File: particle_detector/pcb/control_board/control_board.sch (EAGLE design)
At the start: 35 parts, among them IC1 LT1807R, IC2 SENSL-SIPM, IC3 LT3461, IC4 TEENSY_3.2_NO_BOTTOM

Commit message: move to eagle project; fix vcc/3.3v and ind package; remove full board design
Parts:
- removed C10, C11, C12, C13: (no value), rcl:C-EUC0805K
- removed IC2: SENSL-SIPM, personal:SENSL-SIPM
- removed R11, R12: (no value), rcl:R-EU_M0805
- removed XCHIP: (no value), personal:XCHIP-1X5
- added I2C: (no value), pinhead:PINHD-1X5
- added SIPM: (no value), pinhead:PINHD-2X3
- added XBUS: (no value), personal:XINABOX-XBUS
- C1: value (none) -> 22pF
- C2: value (none) -> 0.47uF
- C3, C4: value (none) -> 1uF
- C5: value (none) -> 10pF
- C6: value (none) -> 10uF
- C7: value (none) -> 0.1uF
- C8: value (none) -> 20nF
- C9, R10: value (none) -> sh
- D1, D2: value B340A -> MBR0540
- IC4: value TEENSY_3.2_NO_BOTTOM -> TEENSY 3.2
- L1: value (none) -> 47uH; device rcl:L-USL2012C -> rcl:L-USL3225M
- L2: value (none) -> 2.5k
- R1, R5, R6: value (none) -> 10k
- R2: value (none) -> 226k
- R3: value (none) -> 1k
- R4: value (none) -> 249
- R7, R8: value (none) -> 100k
- R9: value (none) -> 24.9k
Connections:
- removed net N$5: C11.1, C12.1, C13.1, IC2.CATHODE, R12.2
- removed net N$6: C10.1, R11.2, R12.1
- new net 3.3V: C6.1, C7.1, I2C.4, IC1P.V+, IC4.3.3V, XBUS.3.3V
- new net AGND: C6.2, C7.2, C8.2, IC1P.V-, IC4.AGND, R4.1, R6.1, R7.1, R9.1
- new net SCL: I2C.1, IC4.19/A5/T/SCL0, XBUS.SCL
- new net SDA: I2C.2, IC4.18/A4/T/SDA0, XBUS.SDA
- new net VBAT: XBUS.VBAT
- net GND: now also I2C.3, SIPM.3, SIPM.4, XBUS.GND; no longer C10.2, C11.2, C12.2, C13.2, C6.2, C7.2, C8.2, IC1P.V-, R4.1, R6.1, R7.1, R9.1
- net HV: now also SIPM.1, SIPM.2; no longer R11.1
- net SIGNAL: now also SIPM.5, SIPM.6; no longer IC2.ANODE
- net VCC: now also I2C.5; no longer C6.1, C7.1, IC1P.V+
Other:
- note removed: "SiPM PCB"
- moved on the sheet: C1, C5, IC1P, R4

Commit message: Stuck the TLV on there, not finished
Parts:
- added C10, C11: (no value), rcl:C-EUC0805
- added R11, R12: (no value), resistor:R-EU_M0805
- added U$1: TLV3501, AU_Thinsat_Comparators:TLV3501
- IC1: device personal:LT1807R -> Personal:LT1807R
- IC3: device personal:LT3461 -> Personal:LT3461
- IC4: device personal:TEENSY_3.2_NO_BOTTOM -> Personal:TEENSY_3.2_NO_BOTTOM
- XBUS: device personal:XINABOX-XBUS -> Personal:XINABOX-XBUS
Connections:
- new net INT_TRIG: IC4.22/A8/T/PWM, U$1.OUT
- new net N$5: R11.2, R12.2, U$1.IN-
- net 3.3V: now also C10.1, C11.1, R12.1, U$1.V+
- net GND: now also C10.2, C11.2, R11.1, U$1.SHDN, U$1.V-
- net SIG_PEAK: now also U$1.IN+
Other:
- moved on the sheet: I2C, TOUCH, XBUS

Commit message: reroute traces and fix footprint for TLV chip
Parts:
- removed U$1: TLV3501, AU_Thinsat_Comparators:TLV3501
- added IC2: TLV3501, AU_Thinsat_Comparators:TLV3501
- C10: value (none) -> 10uF
- C11: value (none) -> 0.1uF
- IC1: device Personal:LT1807R -> personal:LT1807R
- IC3: device Personal:LT3461 -> personal:LT3461
- IC4: device Personal:TEENSY_3.2_NO_BOTTOM -> personal:TEENSY_3.2_NO_BOTTOM
- R11: value (none) -> 1k
- R12: value (none) -> 100k
- TOUCH: device pinhead:PINHD-1X3 -> pinhead:PINHD-1X4
- XBUS: device Personal:XINABOX-XBUS -> personal:XINABOX-XBUS
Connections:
- removed net INT_TRIG: IC4.22/A8/T/PWM, U$1.OUT
- new net SIG_INT: IC2.OUT, IC4.22/A8/T/PWM, TOUCH.4
- net 3.3V: now also IC2.V+; no longer U$1.V+
- net AGND: now also C10.2, C11.2, IC2.SHDN, IC2.V-, R11.1
- net GND: no longer C10.2, C11.2, R11.1, U$1.SHDN, U$1.V-
- net N$5: now also IC2.IN-; no longer U$1.IN-
- net SIG_PEAK: now also IC2.IN+; no longer U$1.IN+
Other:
- note added: "Authors: Kristof Aldenderfer, Jacob VanCampen"
- note added: "Detector Board Header"
- note added: "I2C and Xinabox Header"
- note added: "Interrupt Generation"
- note removed: "Author: Kristof Aldenderfer Forked from Cosmic Watch v2"
- moved on the sheet: C10, C11, C5, C6, C7, C8, C9, D1, D2, I2C, IC1A, IC1B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

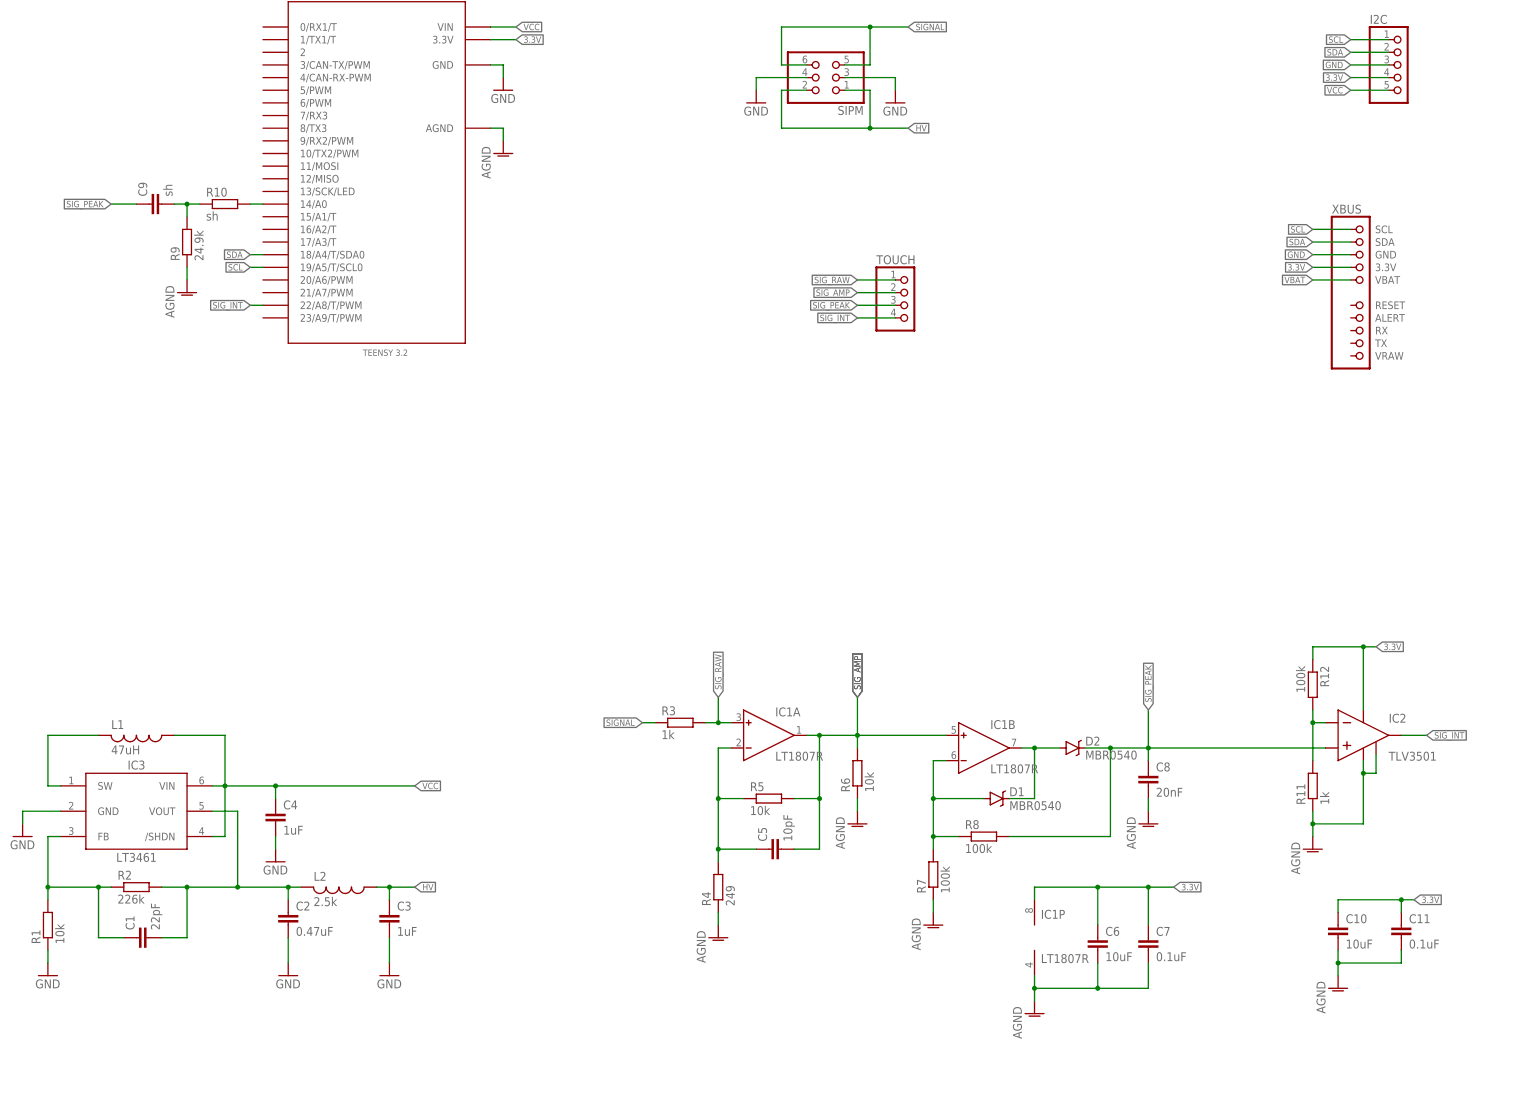
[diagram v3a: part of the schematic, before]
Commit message: remove VCC traces to DC-DC booster; 3.3V traces remain unrouted
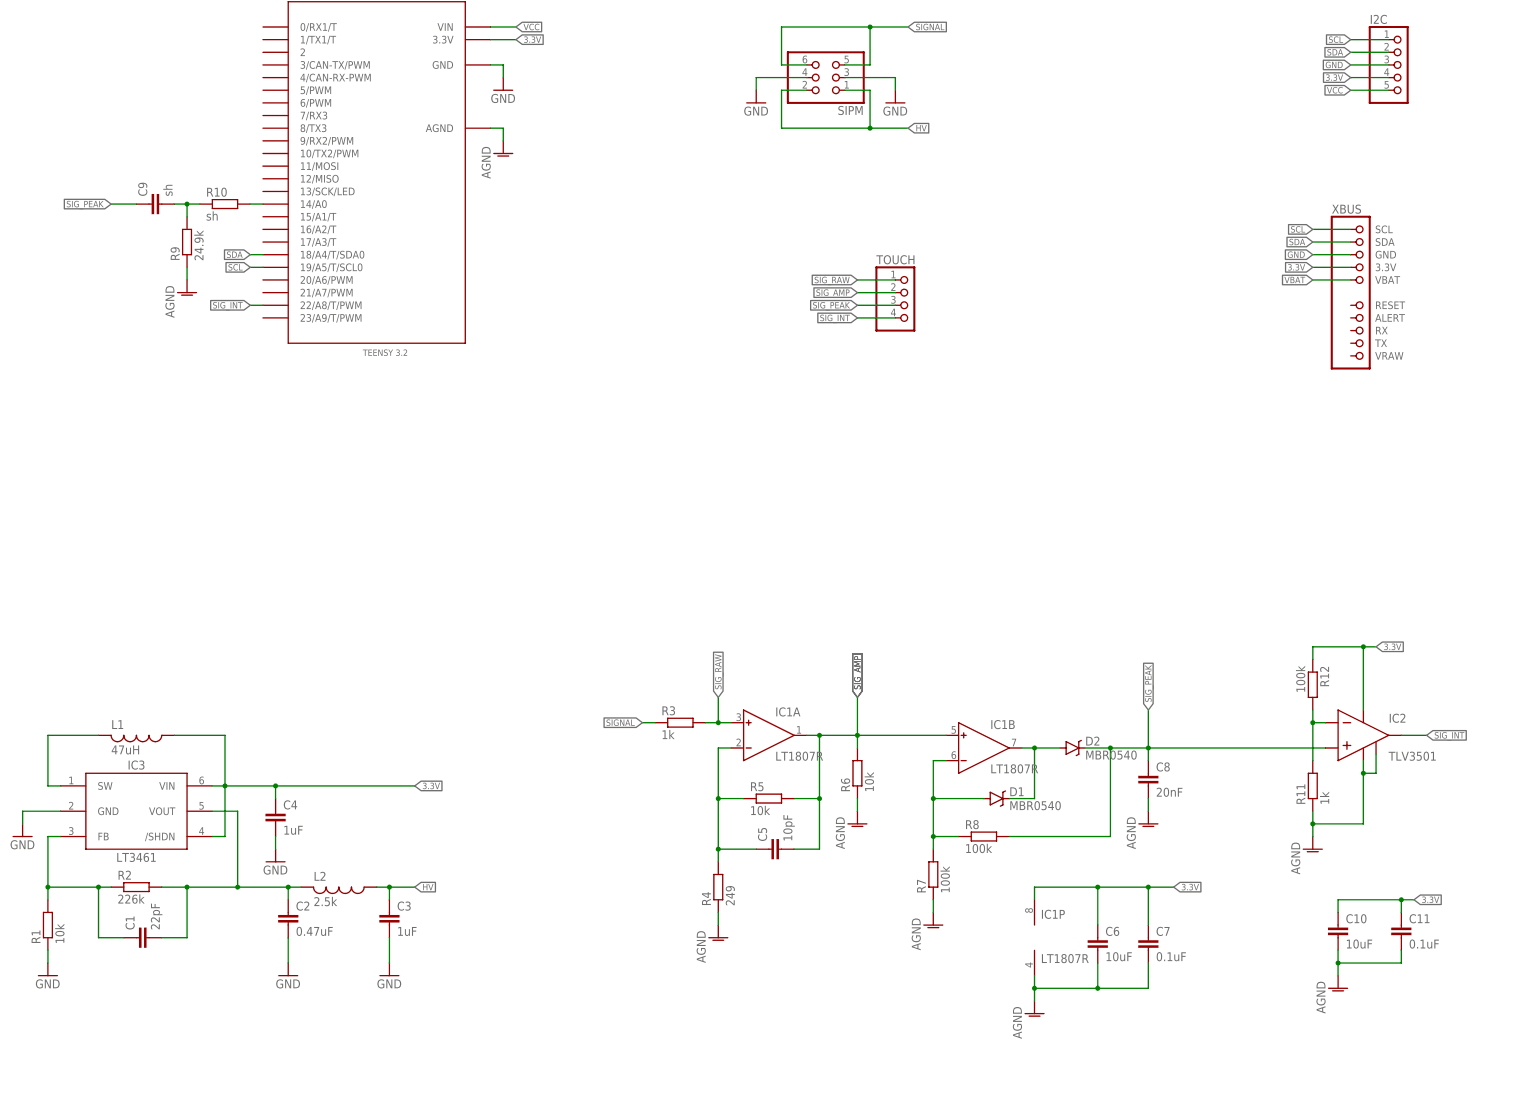
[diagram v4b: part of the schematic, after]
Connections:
- net 3.3V: now also C4.1, IC3./SHDN, IC3.VIN, L1.1
- net VCC: no longer C4.1, IC3./SHDN, IC3.VIN, L1.1

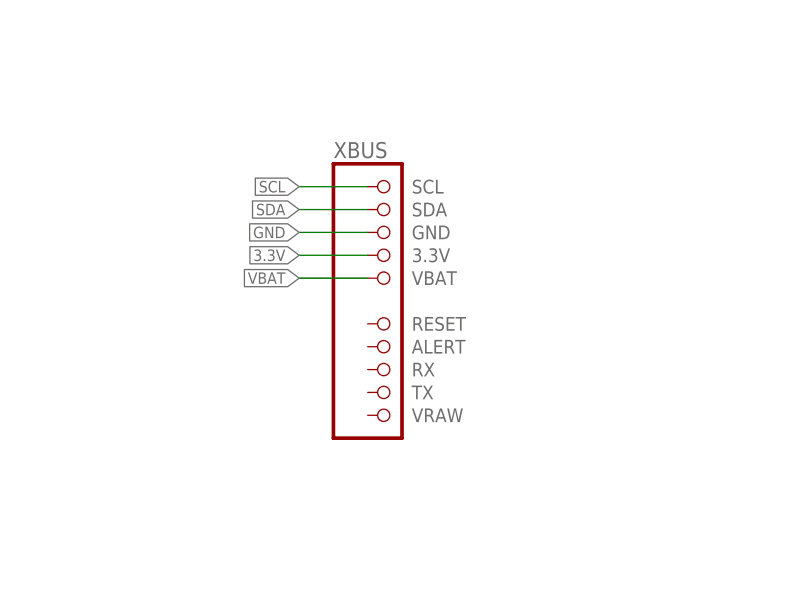
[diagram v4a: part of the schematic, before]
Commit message: adjust comparator footprint; route 3.3V traces. send to fab
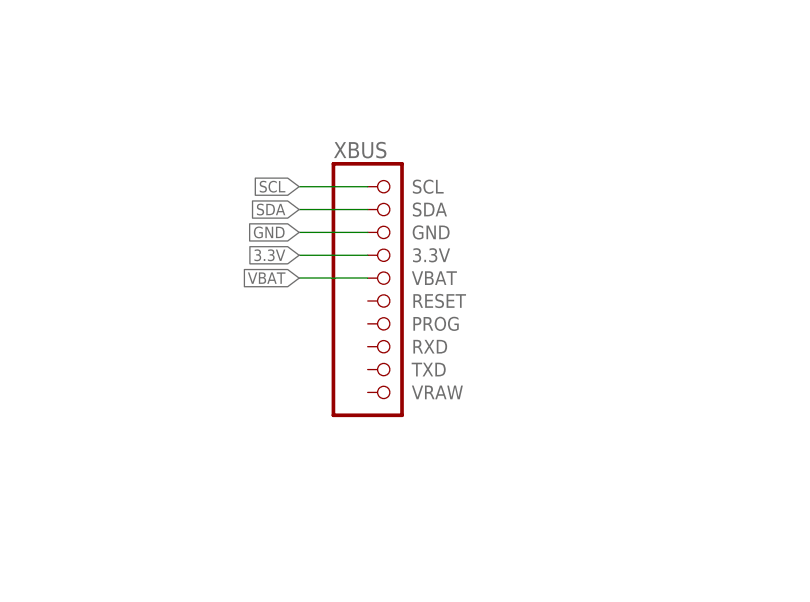
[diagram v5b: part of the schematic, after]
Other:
- moved on the sheet: XBUS

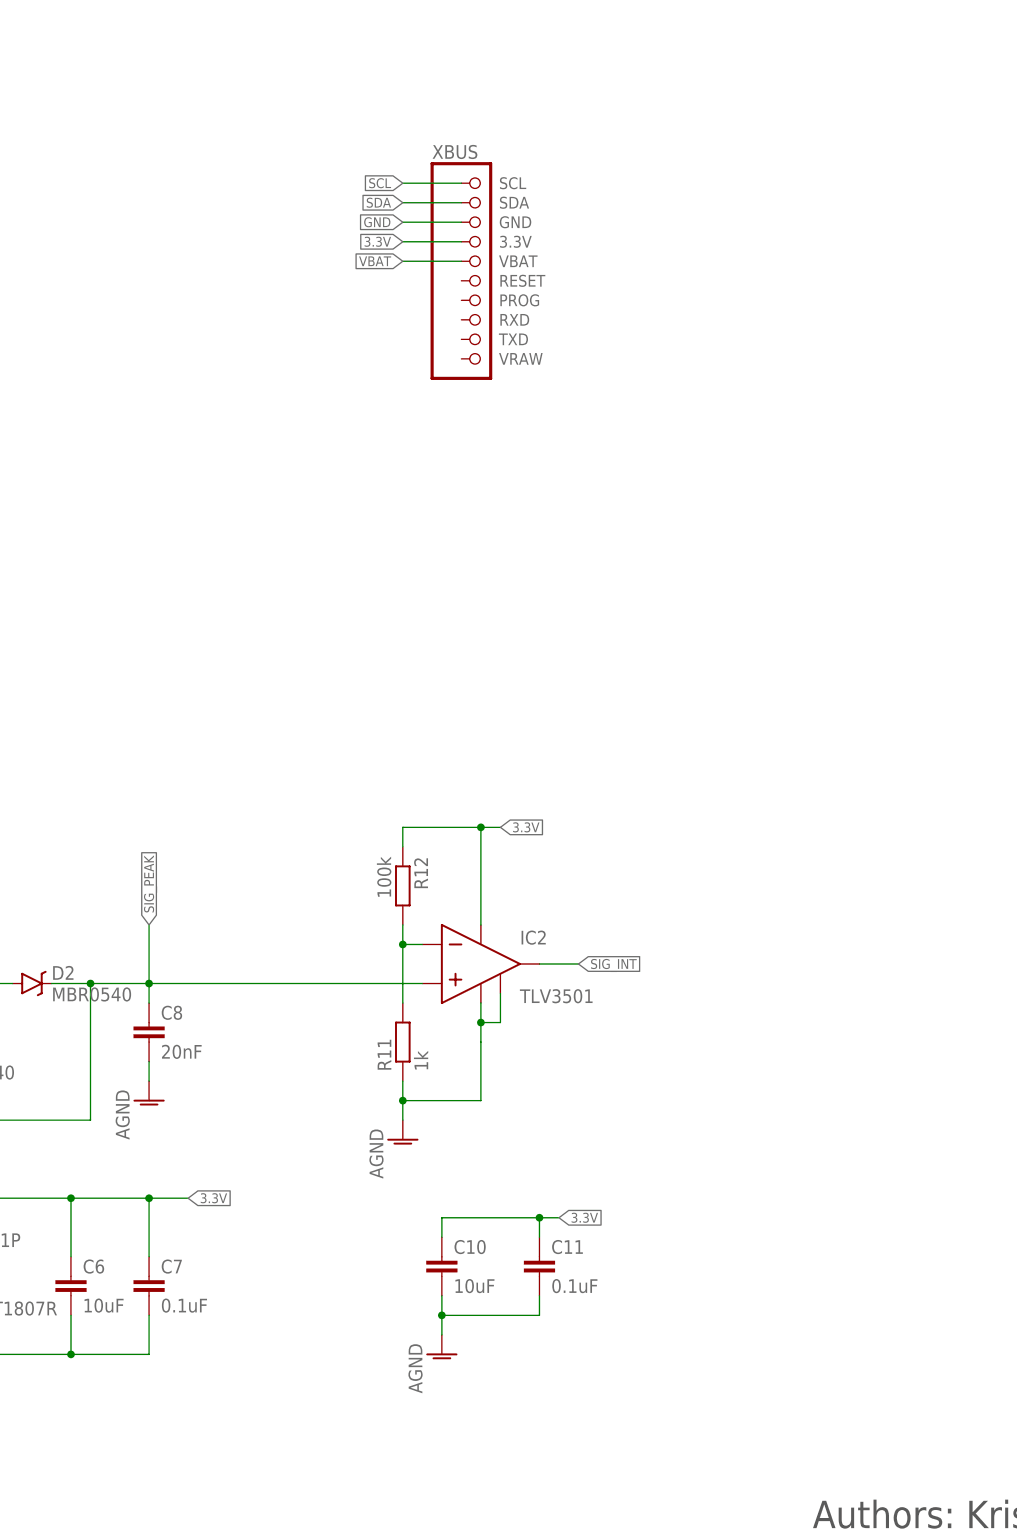
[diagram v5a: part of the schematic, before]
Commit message: begin fix of INT section
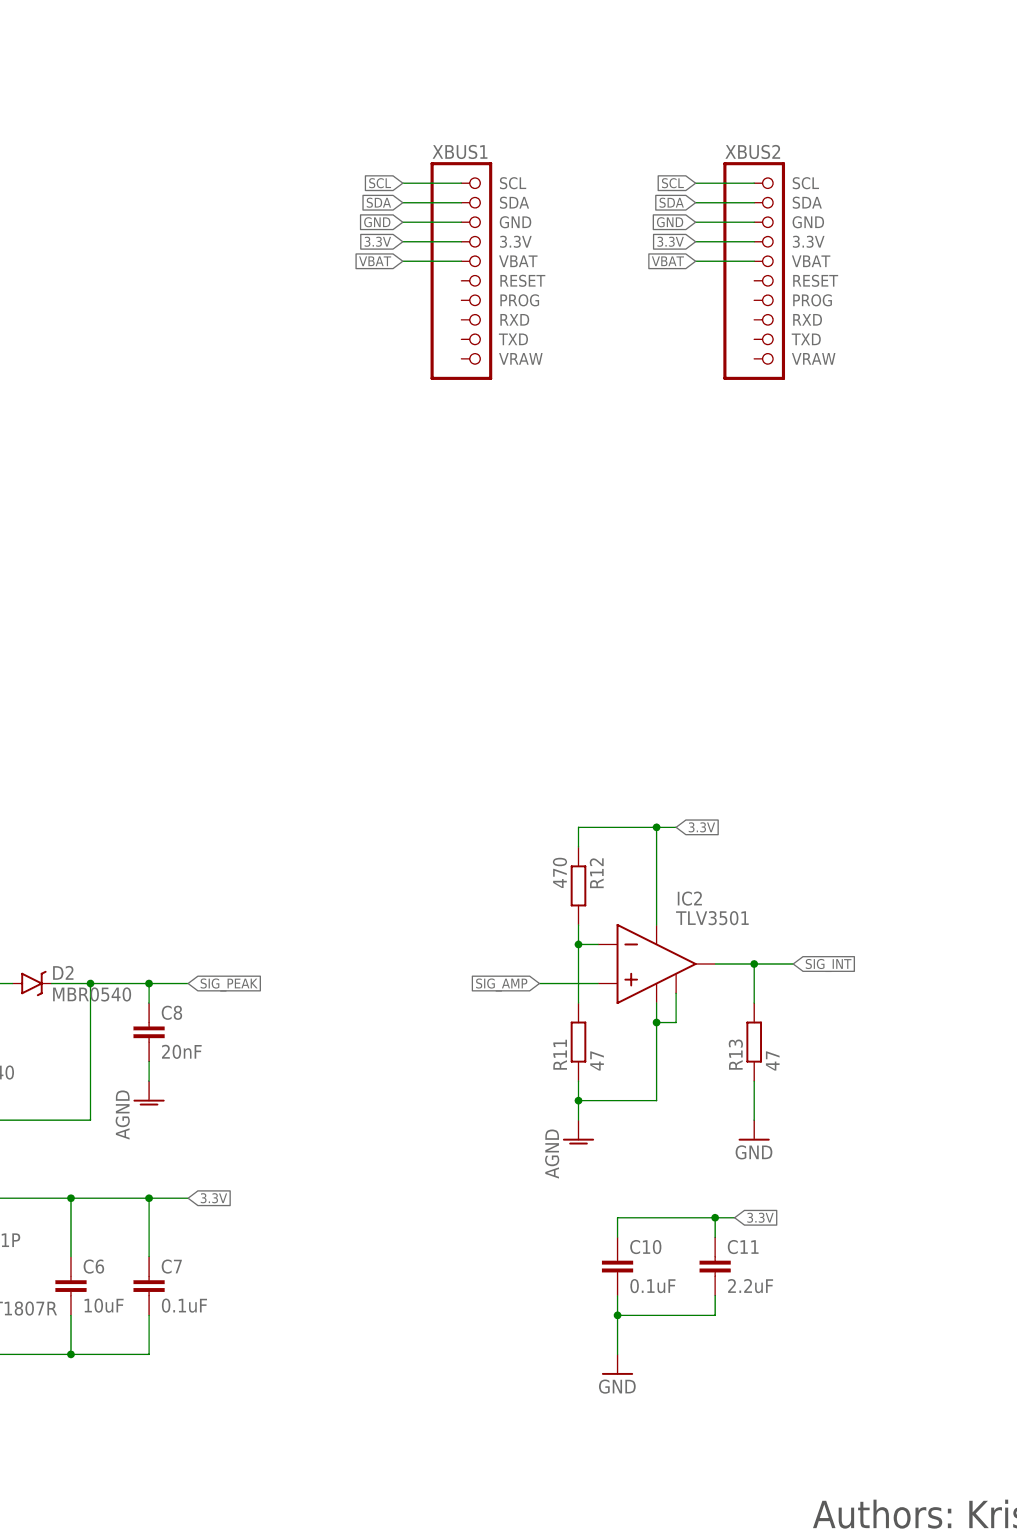
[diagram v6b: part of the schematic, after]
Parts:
- added R13: 47, resistor:R-EU_M0805
- added XBUS2: (no value), personal:XINABOX-XBUS
- C10: value 10uF -> 0.1uF
- C11: value 0.1uF -> 2.2uF
- R11: value 1k -> 47
- R12: value 100k -> 470
- renumbered XBUS to XBUS1
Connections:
- net 3.3V: now also XBUS2.3.3V
- net AGND: no longer C10.2, C11.2
- net GND: now also C10.2, C11.2, R13.1, XBUS2.GND
- net SCL: now also XBUS2.SCL
- net SDA: now also XBUS2.SDA
- net SIG_AMP: now also IC2.IN+
- net SIG_INT: now also R13.2
- net SIG_PEAK: no longer IC2.IN+
- net VBAT: now also XBUS2.VBAT
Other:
- moved on the sheet: C10, C11, IC2, R11, R12
